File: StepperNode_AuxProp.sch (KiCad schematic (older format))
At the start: 7 parts

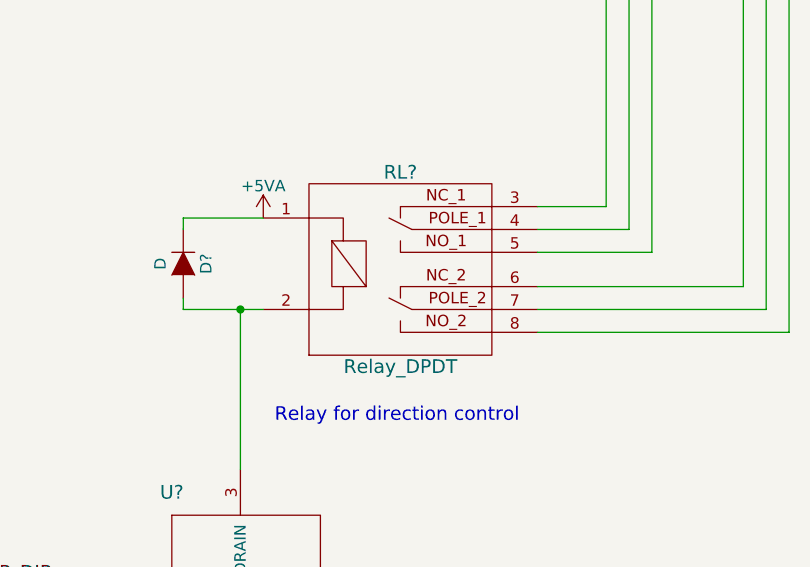
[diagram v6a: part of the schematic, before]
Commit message: Update DAC's and routed gimbal position to MCU direct.
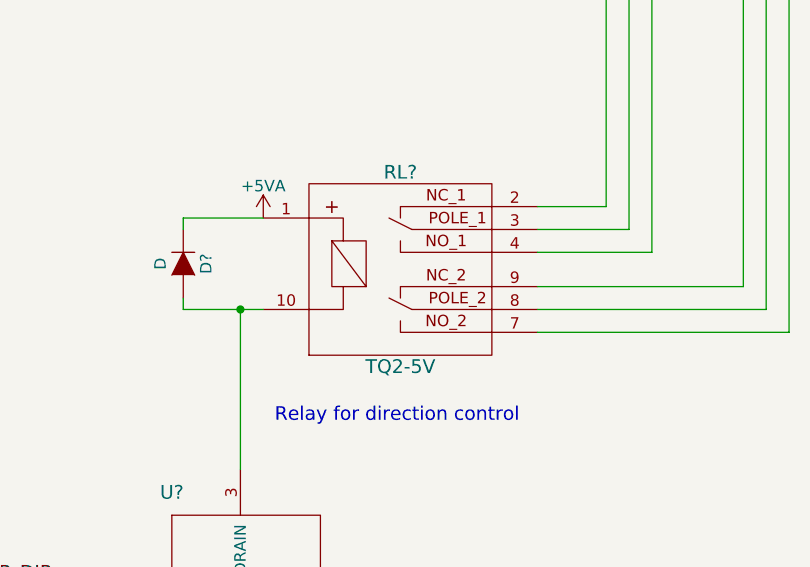
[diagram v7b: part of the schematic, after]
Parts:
- removed RL?: Relay_DPDT, symbol Relay_DPDT
- removed U?: NUD3124LT1G, symbol NUD3124LT1G
- added RL?: TQ2-5V, symbol TQ2-5V
- added U?: NUD3124LT1G, RLOOP_FOOTPRINTS:rLoop_SOT23, symbol NUD3124LT1G
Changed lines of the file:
@@
-	1    0    0    -1
-$EndComp
-$Comp
-L Relay_DPDT RL?
-U 1 1 575AEE52
-P 9900 7100
-F 0 "RL?" H 10300 7900 60  0000 C CNN
-F 1 "Relay_DPDT" H 10300 7050 60  0000 C CNN
-F 2 "" H 9900 7100 60  0000 C CNN
-F 3 "" H 9900 7100 60  0000 C CNN
-	1    9900 7100
 	1    0    0    -1
 $EndComp
@@
 AUXPROP_DIR
 $Comp
-L NUD3124LT1G U?
-U 1 1 575D421F
-P 9300 7800
-F 0 "U?" H 9300 7900 60  0000 C CNN
-F 1 "NUD3124LT1G" H 10000 7150 60  0000 C CNN
-F 2 "" H 9300 7800 60  0000 C CNN
-F 3 "" H 9300 7800 60  0000 C CNN
-	1    9300 7800
-	1    0    0    -1
-$EndComp
-$Comp
 L D D?
 U 1 1 575D425E
@@
 Text Notes 8850 1700 0    118  ~ 0
 TODO: CHECK ELECTRICAL ISOLATION OF RAGEBRIDGE CONTROLLER
+$Comp
+L NUD3124LT1G U?
+U 1 1 575A6F17
+P 9300 7800
+F 0 "U?" H 9300 7900 60  0000 C CNN
+F 1 "NUD3124LT1G" H 10000 7150 60  0000 C CNN
+F 2 "RLOOP_FOOTPRINTS:rLoop_SOT23" H 9200 7800 60  0001 C CNN
+F 3 "" H 9300 7800 60  0000 C CNN
+	1    9300 7800
+	1    0    0    -1
+$EndComp
+$Comp
+L TQ2-5V RL?
+U 1 1 575A07B2
+P 9900 6350
+F 0 "RL?" H 10300 6400 60  0000 C CNN
+F 1 "TQ2-5V" H 10300 5550 60  0000 C CNN
+F 2 "" H 9900 5600 60  0000 C CNN
+F 3 "" H 9900 5600 60  0000 C CNN
+	1    9900 6350
+	1    0    0    -1
+$EndComp
 $EndSCHEMATC

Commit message: First Revision -
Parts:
- removed D?: D, symbol D
- removed P? (x2): CONN_01X08_2MNT, symbol CONN_01X08_2MNT
- removed RL?: TQ2-5V, symbol TQ2-5V
- added D2: BAS16,215, RLOOP_FOOTPRINTS:rLoop_SOT23, symbol BAS16,215
- added P10, P11: TE_640456-8, RLOOP_FOOTPRINTS:rLoop_TE640456-8, symbol TE_640456-8
- added RL2: TQ2-5V, RLOOP_FOOTPRINTS:rLoop_DIP10, symbol TQ2-5V
- gave numbers to parts that had none: 3
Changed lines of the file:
@@
 Text Notes 11950 10500 0    60   ~ 0
 Original Author: SafetyLok
-$Comp
-L CONN_01X08_2MNT P?
-U 1 1 575AE559
-P 13800 2650
-F 0 "P?" H 13800 3100 50  0000 C CNN
-F 1 "CONN_01X08_2MNT" V 13900 2650 50  0000 C CNN
-F 2 "" H 13800 2650 50  0000 C CNN
-F 3 "" H 13800 2650 50  0000 C CNN
-	1    13800 2650
-	1    0    0    -1
-$EndComp
 Text Notes 14350 3050 1    60   ~ 0
 Left Aux Prop Motor
@@
 Text HLabel 3850 5450 0    60   Input ~ 0
 B_AP2_THROTTLE
-$Comp
-L CONN_01X08_2MNT P?
-U 1 1 575AEC09
-P 13800 4350
-F 0 "P?" H 13800 4800 50  0000 C CNN
-F 1 "CONN_01X08_2MNT" V 13900 4350 50  0000 C CNN
-F 2 "" H 13800 4350 50  0000 C CNN
-F 3 "" H 13800 4350 50  0000 C CNN
-	1    13800 4350
-	1    0    0    -1
-$EndComp
 Text Notes 9750 7400 0    60   ~ 0
 Relay for direction control
@@
 CHB_AUXPROP_DIR
 $Comp
-L +5VA #PWR?
+L +5VA #PWR122
 U 1 1 5756511D
 P 5750 4850
-F 0 "#PWR?" H 5750 4700 50  0001 C CNN
+F 0 "#PWR122" H 5750 4700 50  0001 C CNN
 F 1 "+5VA" H 5750 4990 50  0000 C CNN
 F 2 "" H 5750 4850 50  0000 C CNN
@@
 $EndComp
 $Comp
-L +5VA #PWR?
+L +5VA #PWR123
 U 1 1 575651A0
 P 6150 4150
-F 0 "#PWR?" H 6150 4000 50  0001 C CNN
+F 0 "#PWR123" H 6150 4000 50  0001 C CNN
 F 1 "+5VA" H 6150 4290 50  0000 C CNN
 F 2 "" H 6150 4150 50  0000 C CNN
@@
 $EndComp
 $Comp
-L GNDA #PWR?
+L GNDA #PWR119
 U 1 1 575651AF
 P 5000 6750
-F 0 "#PWR?" H 5000 6500 50  0001 C CNN
+F 0 "#PWR119" H 5000 6500 50  0001 C CNN
 F 1 "GNDA" H 5000 6600 50  0000 C CNN
 F 2 "" H 5000 6750 50  0000 C CNN
@@
 VinH = 1.6V
 $Comp
-L GNDD #PWR?
+L GNDD #PWR121
 U 1 1 57565359
 P 5550 4850
-F 0 "#PWR?" H 5550 4600 50  0001 C CNN
+F 0 "#PWR121" H 5550 4600 50  0001 C CNN
 F 1 "GNDD" H 5550 4700 50  0000 C CNN
 F 2 "" H 5550 4850 50  0000 C CNN
@@
 Unused Inputs GND
 $Comp
-L GNDA #PWR?
+L GNDA #PWR124
 U 1 1 5756652B
 P 6150 4450
-F 0 "#PWR?" H 6150 4200 50  0001 C CNN
+F 0 "#PWR124" H 6150 4200 50  0001 C CNN
 F 1 "GNDA" H 6150 4300 50  0000 C CNN
 F 2 "" H 6150 4450 50  0000 C CNN
@@
 $EndComp
 $Comp
-L GNDA #PWR?
+L GNDA #PWR120
 U 1 1 5756673C
 P 5500 7250
-F 0 "#PWR?" H 5500 7000 50  0001 C CNN
+F 0 "#PWR120" H 5500 7000 50  0001 C CNN
 F 1 "GNDA" H 5500 7100 50  0000 C CNN
 F 2 "" H 5500 7250 50  0000 C CNN
@@
 AUXPROP_DIR
 $Comp
-L +5VA #PWR?
+L +5VA #PWR126
 U 1 1 575C0D8C
 P 9700 6500
-F 0 "#PWR?" H 9700 6350 50  0001 C CNN
+F 0 "#PWR126" H 9700 6350 50  0001 C CNN
 F 1 "+5VA" H 9700 6640 50  0000 C CNN
 F 2 "" H 9700 6500 50  0000 C CNN
@@
 Text Label 8200 8100 0    60   ~ 0
 AUXPROP_DIR
-$Comp
-L D D?
-U 1 1 575D425E
-P 9350 6700
-F 0 "D?" H 9350 6800 50  0000 C CNN
-F 1 "D" H 9350 6600 50  0000 C CNN
-F 2 "" H 9350 6700 50  0000 C CNN
-F 3 "" H 9350 6700 50  0000 C CNN
-	1    9350 6700
-	0    1    1    0
-$EndComp
 Wire Wire Line
 	9700 6500 9350 6500
@@
 Connection ~ 9600 6900
 $Comp
-L GNDA #PWR?
+L GNDA #PWR125
 U 1 1 575D465A
 P 9600 8600
-F 0 "#PWR?" H 9600 8350 50  0001 C CNN
+F 0 "#PWR125" H 9600 8350 50  0001 C CNN
 F 1 "GNDA" H 9600 8450 50  0000 C CNN
 F 2 "" H 9600 8600 50  0000 C CNN
@@
 Permits direction control (switching)\nof the RageBridge controller
 $Comp
-L GNDA #PWR?
+L GNDA #PWR127
 U 1 1 575D497D
 P 13600 3000
-F 0 "#PWR?" H 13600 2750 50  0001 C CNN
+F 0 "#PWR127" H 13600 2750 50  0001 C CNN
 F 1 "GNDA" H 13600 2850 50  0000 C CNN
 F 2 "" H 13600 3000 50  0000 C CNN
@@
 $EndComp
 $Comp
-L GNDA #PWR?
+L GNDA #PWR128
 U 1 1 575D498C
 P 13600 4700
-F 0 "#PWR?" H 13600 4450 50  0001 C CNN
+F 0 "#PWR128" H 13600 4450 50  0001 C CNN
 F 1 "GNDA" H 13600 4550 50  0000 C CNN
 F 2 "" H 13600 4700 50  0000 C CNN
@@
 	12000 4300 13600 4300
 $Comp
-L MAX4948ETG+ U?
+L MAX4948ETG+ U19
 U 1 1 575A2A8F
 P 5200 5050
-F 0 "U?" H 6050 5100 60  0000 C CNN
+F 0 "U19" H 6050 5100 60  0000 C CNN
 F 1 "MAX4948ETG+" H 6250 3200 60  0000 C CNN
 F 2 "RLOOP_FOOTPRINTS:rLoop_QFN24_4x4mm" H 5200 4000 60  0001 C CNN
@@
 $EndComp
 $Comp
-L C_100nF_50V C?
+L C_100nF_50V C29
 U 1 1 575A2AEB
 P 6150 4300
-F 0 "C?" H 6175 4400 50  0000 L CNN
+F 0 "C29" H 6175 4400 50  0000 L CNN
 F 1 "C_100nF_50V" H 6175 4200 50  0000 L CNN
 F 2 "RLOOP_FOOTPRINTS:rLoop_C_0603" H 6188 4150 50  0001 C CNN
@@
 TODO: CHECK ELECTRICAL ISOLATION OF RAGEBRIDGE CONTROLLER
 $Comp
-L NUD3124LT1G U?
+L NUD3124LT1G U20
 U 1 1 575A6F17
 P 9300 7800
-F 0 "U?" H 9300 7900 60  0000 C CNN
+F 0 "U20" H 9300 7900 60  0000 C CNN
 F 1 "NUD3124LT1G" H 10000 7150 60  0000 C CNN
 F 2 "RLOOP_FOOTPRINTS:rLoop_SOT23" H 9200 7800 60  0001 C CNN
@@
 $EndComp
 $Comp
-L TQ2-5V RL?
-U 1 1 575A07B2
+L BAS16,215 D2
+U 1 1 5765E1F8
+P 9350 6700
+F 0 "D2" H 9350 6800 50  0000 C CNN
+F 1 "BAS16,215" H 9350 6600 50  0000 C CNN
+F 2 "RLOOP_FOOTPRINTS:rLoop_SOT23" H 9250 6700 50  0001 C CNN
+F 3 "" H 9350 6700 50  0000 C CNN
+	1    9350 6700
+	0    1    1    0
+$EndComp
+$Comp
+L TQ2-5V RL2
+U 1 1 5765E2D8
 P 9900 6350
-F 0 "RL?" H 10300 6400 60  0000 C CNN
+F 0 "RL2" H 10300 6400 60  0000 C CNN
 F 1 "TQ2-5V" H 10300 5550 60  0000 C CNN
-F 2 "" H 9900 5600 60  0000 C CNN
+F 2 "RLOOP_FOOTPRINTS:rLoop_DIP10" H 9900 5600 60  0001 C CNN
 F 3 "" H 9900 5600 60  0000 C CNN
 	1    9900 6350
 	1    0    0    -1
 $EndComp
+$Comp
+L TE_640456-8 P10
+U 1 1 5765E443
+P 13750 2250
+F 0 "P10" H 13800 2300 50  0000 C CNN
+F 1 "TE_640456-8" V 13900 1850 50  0000 C CNN
+F 2 "RLOOP_FOOTPRINTS:rLoop_TE640456-8" H 13800 1850 50  0001 C CNN
+F 3 "" H 13800 1850 50  0000 C CNN
+	1    13750 2250
+	1    0    0    -1
+$EndComp
+$Comp
+L TE_640456-8 P11
+U 1 1 5765E4D2
+P 13750 3950
+F 0 "P11" H 13800 4000 50  0000 C CNN
+F 1 "TE_640456-8" V 13900 3550 50  0000 C CNN
+F 2 "RLOOP_FOOTPRINTS:rLoop_TE640456-8" H 13800 3550 50  0001 C CNN
+F 3 "" H 13800 3550 50  0000 C CNN
+	1    13750 3950
+	1    0    0    -1
+$EndComp
